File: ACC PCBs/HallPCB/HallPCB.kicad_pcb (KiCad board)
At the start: 2 copper layers, 22.8 x 11.3 mm, 3 parts, among them J1 Conn_01x04_Socket, U2 AP2127N-1.0

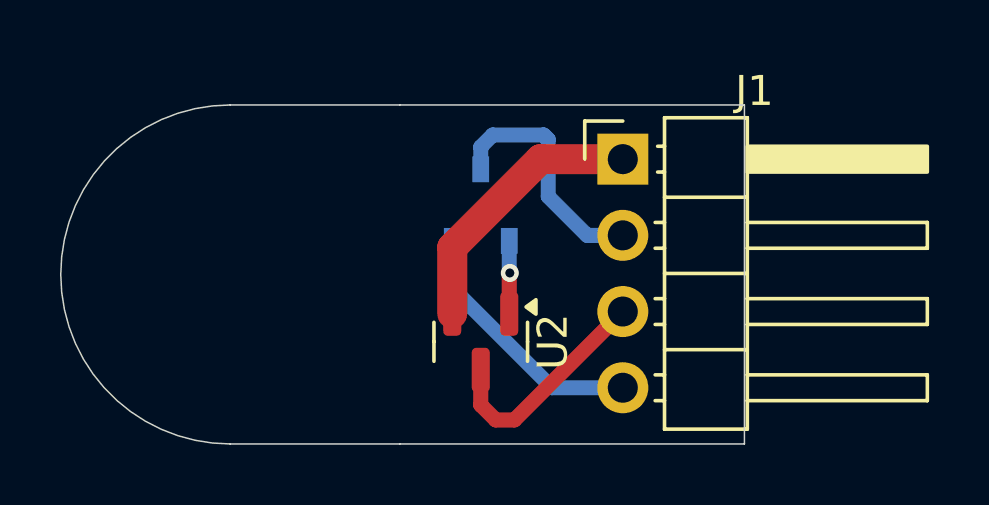
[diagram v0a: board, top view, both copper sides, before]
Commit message: post R1 - flipped many traces and worked on adding an internal sensor for reduncancy
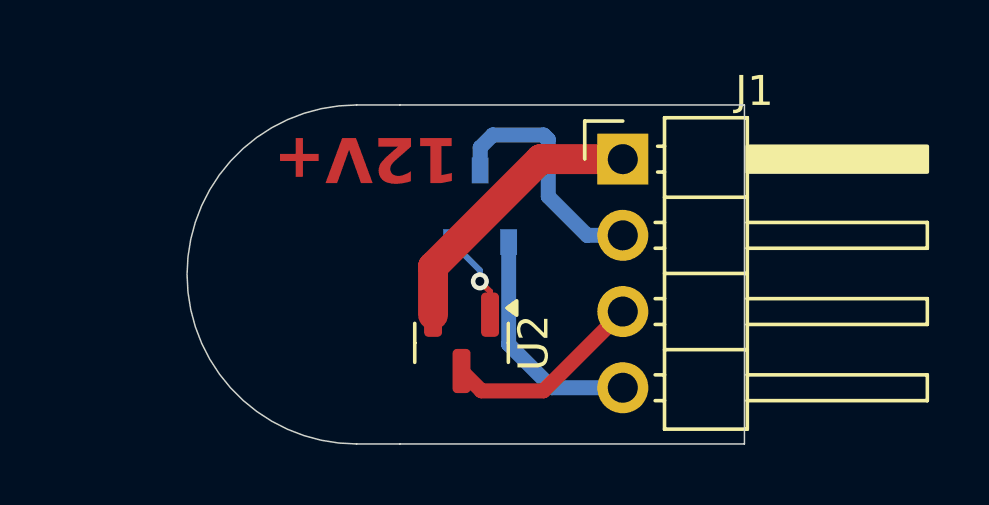
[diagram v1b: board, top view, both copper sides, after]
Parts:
- moved U2 0.64 mm to (135.4, 85.6)
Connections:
- HALL pad 1: SIG -> VOUT
- HALL pad 2: VOUT -> SIG
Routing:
- net RAWSWPOWER: track 7.61 -> 6.74 mm
- net VOUT: track 8.63 -> 7.81 mm
- net SIG: track 2.44 -> 2.95 mm
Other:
- board size 22.8 x 11.3 mm -> 18.6 x 11.3 mm
- board text added: "12V+"
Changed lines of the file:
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@@
 			(drillshape 0)
 			(scaleselection 1)
-			(outputdirectory "FAB/")
+			(outputdirectory "../../../Downloads/PWROUTPUT/")
 		)
 	)
@@
 	(footprint "Package_TO_SOT_SMD:SOT-23"
 		(layer "F.Cu")
-		(at 136 85.5947 -90)
+		(at 135.36 85.63 -90)
 		(descr "SOT, 3 Pin (JEDEC TO-236 Var AB https://www.jedec.org/document_search?search_api_views_fulltext=TO-236), generated with kicad-footprint-generator ipc_gullwing_generator.py")
 		(tags "SOT TO_SOT_SMD")
@@
 	(footprint "TLE49643MXTMA1:PG-SOT23-3-15_INF"
 		(layer "B.Cu")
-		(at 136 81.0385 90)
+		(at 135.980001 81.0762 90)
 		(tags "TLE49643MXTMA1 ")
 		(property "Reference" "HALL"
-			(at 0 0 0)
+			(at 0 -2.440001 270)
 			(unlocked yes)
 			(layer "B.SilkS")
@@
 		)
 		(property "Datasheet" "https://www.infineon.com/dgdl/Infineon-TLE4964_3M-DS-v01_00-en.pdf?fileId=db3a30433cabdd35013cc94b7c0f64f9"
-			(at 0 0 270)
+			(at 0 0 90)
 			(layer "B.Fab")
 			(hide yes)
@@
 		)
 		(property "Description" ""
-			(at 0 0 270)
+			(at 0 0 90)
 			(layer "B.Fab")
 			(hide yes)
@@
 		(attr smd)
 		(fp_line
+			(start 0.8255 -1.6256)
+			(end 0.8255 -0.61214)
+			(stroke
+				(width 0.1524)
+				(type solid)
+			)
+			(layer "B.SilkS")
+		)
+		(fp_line
+			(start -0.8255 -1.6256)
+			(end 0.8255 -1.6256)
+			(stroke
+				(width 0.1524)
+				(type solid)
+			)
+			(layer "B.SilkS")
+		)
+		(fp_line
 			(start -0.8255 0.337861)
 			(end -0.8255 -0.337861)
+			(stroke
+				(width 0.1524)
+				(type solid)
+			)
+			(layer "B.SilkS")
+		)
+		(fp_line
+			(start 0.8255 0.61214)
+			(end 0.8255 1.6256)
+			(stroke
+				(width 0.1524)
+				(type solid)
+			)
+			(layer "B.SilkS")
+		)
+		(fp_line
+			(start 0.8255 1.6256)
+			(end -0.8255 1.6256)
 			(stroke
 				(width 0.1524)
@@
 		)
 		(fp_text user "*"
+			(at -1.4478 2.6518 90)
+			(layer "B.SilkS")
+			(effects
+				(font
+					(size 1 1)
+					(thickness 0.15)
+				)
+				(justify mirror)
+			)
+		)
+		(fp_text user "*"
 			(at -1.4478 2.6518 270)
 			(unlocked yes)
@@
 			)
 		)
+		(fp_text user "${REFERENCE}"
+			(at 0 0 270)
+			(unlocked yes)
+			(layer "B.Fab")
+			(effects
+				(font
+					(size 1 1)
+					(thickness 0.15)
+				)
+				(justify mirror)
+			)
+		)
 		(fp_text user "*"
-			(at -1.4478 2.6518 270)
-			(layer "B.SilkS")
+			(at -0.3175 1.4224 90)
+			(layer "B.Fab")
 			(effects
 				(font
@@
 		(fp_text user "*"
 			(at -0.3175 1.4224 270)
-			(unlocked yes)
-			(layer "B.Fab")
-			(effects
-				(font
-					(size 1 1)
-					(thickness 0.15)
-				)
-				(justify mirror)
-			)
-		)
-		(fp_text user "*"
-			(at -0.3175 1.4224 270)
-			(layer "B.Fab")
-			(effects
-				(font
-					(size 1 1)
-					(thickness 0.15)
-				)
-				(justify mirror)
-			)
-		)
-		(fp_text user "${REFERENCE}"
-			(at 0 0 270)
 			(unlocked yes)
 			(layer "B.Fab")
@@
 			(size 0.8636 0.5588)
 			(layers "B.Cu" "B.Mask" "B.Paste")
-			(net 5 "SIG")
+			(net 2 "VOUT")
 			(pinfunction "VDD")
 			(pintype "power_in")
@@
 			(size 0.8636 0.5588)
 			(layers "B.Cu" "B.Mask" "B.Paste")
-			(net 2 "VOUT")
+			(net 5 "SIG")
 			(pinfunction "Q")
 			(pintype "output")
@@
 	)
 	(gr_line
+		(start 133.3 89)
+		(end 131.86 89)
+		(stroke
+			(width 0.05)
+			(type default)
+		)
+		(layer "Edge.Cuts")
+	)
+	(gr_line
 		(start 144.789524 89)
 		(end 144.789524 77.7)
@@
 	)
 	(gr_line
-		(start 127.65 77.7)
-		(end 133.3 77.7)
-		(stroke
-			(width 0.05)
-			(type default)
-		)
-		(layer "Edge.Cuts")
-	)
-	(gr_line
-		(start 127.65 89)
-		(end 133.3 89)
+		(start 133.3 77.7)
+		(end 131.86 77.7)
 		(stroke
 			(width 0.05)
@@
 	)
 	(gr_arc
-		(start 127.65 89)
-		(mid 122 83.35)
-		(end 127.65 77.7)
+		(start 131.86 89)
+		(mid 126.21 83.35)
+		(end 131.86 77.7)
 		(stroke
 			(width 0.05)
@@
 		)
 		(layer "Edge.Cuts")
+	)
+	(gr_text "12V+\n"
+		(at 135.27 78.62 180)
+		(layer "F.Cu")
+		(effects
+			(font
+				(size 1.5 1.5)
+				(thickness 0.3)
+				(bold yes)
+			)
+			(justify left bottom)
+		)
+	)
+	(segment
+		(start 136.4 78.7)
+		(end 135.980001 79.119999)
+		(width 0.5)
+		(layer "B.Cu")
+		(net 1)
+	)
+	(segment
+		(start 140.7354 82.0462)
+		(end 139.5462 82.0462)
+		(width 0.5)
+		(layer "B.Cu")
+		(net 1)
+	)
+	(segment
+		(start 138.25 80.75)
+		(end 138.25 78.85)
+		(width 0.5)
+		(layer "B.Cu")
+		(net 1)
+	)
+	(segment
+		(start 138.1 78.7)
+		(end 136.4 78.7)
+		(width 0.5)
+		(layer "B.Cu")
+		(net 1)
+	)
+	(segment
+		(start 135.980001 79.119999)
+		(end 135.980001 79.8824)
+		(width 0.5)
+		(layer "B.Cu")
+		(net 1)
+	)
+	(segment
+		(start 139.5462 82.0462)
+		(end 138.25 80.75)
+		(width 0.5)
+		(layer "B.Cu")
+		(net 1)
 	)
 	(segment
@@
 	)
 	(segment
-		(start 139.5462 82.0462)
-		(end 138.25 80.75)
-		(width 0.5)
-		(layer "B.Cu")
-		(net 1)
-	)
-	(segment
-		(start 136.4 78.7)
-		(end 136 79.1)
-		(width 0.5)
-		(layer "B.Cu")
-		(net 1)
-	)
-	(segment
-		(start 138.1 78.7)
-		(end 136.4 78.7)
-		(width 0.5)
-		(layer "B.Cu")
-		(net 1)
-	)
-	(segment
-		(start 136 79.1)
-		(end 136 79.8447)
-		(width 0.5)
-		(layer "B.Cu")
-		(net 1)
-	)
-	(segment
-		(start 140.7354 82.0462)
-		(end 139.5462 82.0462)
-		(width 0.5)
-		(layer "B.Cu")
-		(net 1)
-	)
-	(segment
-		(start 138.25 80.75)
-		(end 138.25 78.85)
-		(width 0.5)
-		(layer "B.Cu")
-		(net 1)
-	)
-	(segment
-		(start 135.049999 83.799999)
-		(end 135.049999 82.2323)
+		(start 136.930002 85.680002)
+		(end 136.930002 82.27)
 		(width 0.5)
 		(layer "B.Cu")
@@
 	(segment
 		(start 138.3762 87.1262)
-		(end 135.049999 83.799999)
+		(end 136.930002 85.680002)
 		(width 0.5)
 		(layer "B.Cu")
@@
 	)
 	(segment
-		(start 140.7354 84.5862)
-		(end 137.1216 88.2)
+		(start 136.0225 87.23)
+		(end 135.36 86.5675)
 		(width 0.5)
 		(layer "F.Cu")
@@
 	)
 	(segment
-		(start 136 87.7)
-		(end 136 86.5322)
+		(start 138.0916 87.23)
+		(end 136.0225 87.23)
 		(width 0.5)
 		(layer "F.Cu")
@@
 	)
 	(segment
-		(start 137.1216 88.2)
-		(end 136.5 88.2)
+		(start 140.7354 84.5862)
+		(end 138.0916 87.23)
 		(width 0.5)
 		(layer "F.Cu")
@@
 	)
 	(segment
-		(start 136.5 88.2)
-		(end 136 87.7)
-		(width 0.5)
-		(layer "F.Cu")
-		(net 3)
-	)
-	(segment
-		(start 135.05 82.45)
-		(end 135.05 84.6572)
-		(width 1)
-		(layer "F.Cu")
-		(net 4)
-	)
-	(segment
-		(start 135.05 82.45)
-		(end 137.9938 79.5062)
+		(start 134.41 83.09)
+		(end 134.41 84.6925)
 		(width 1)
 		(layer "F.Cu")
@@
 	)
 	(segment
-		(start 137.9938 79.5062)
-		(end 140.7354 79.5062)
+		(start 140.7354 79.5062)
+		(end 137.9938 79.5062)
 		(width 1)
 		(layer "F.Cu")
@@
 	)
 	(segment
-		(start 136.95 83.318964)
-		(end 136.968964 83.3)
-		(width 0.5)
+		(start 137.9938 79.5062)
+		(end 134.41 83.09)
+		(width 1)
+		(layer "F.Cu")
+		(net 4)
+	)
+	(segment
+		(start 136.31 84.6925)
+		(end 136.31 83.92)
+		(width 0.2)
 		(layer "F.Cu")
 		(net 5)
 	)
 	(segment
-		(start 136.95 84.6572)
-		(end 136.95 83.318964)
-		(width 0.5)
+		(start 136.31 83.92)
+		(end 135.97 83.58)
+		(width 0.2)
 		(layer "F.Cu")
 		(net 5)
 	)
 	(via
-		(at 136.968964 83.3)
+		(at 135.97 83.58)
 		(size 0.6)
 		(drill 0.3)
 		(layers "F.Cu" "B.Cu")
-		(free yes)
 		(net 5)
 	)
 	(segment
-		(start 136.950001 82.2323)
-		(end 136.950001 83.281037)
-		(width 0.5)
+		(start 135.97 83.58)
+		(end 135.97 83.21)
+		(width 0.2)
 		(layer "B.Cu")
 		(net 5)
 	)
 	(segment
-		(start 136.950001 83.281037)
-		(end 136.968964 83.3)
-		(width 0.5)
+		(start 135.97 83.21)
+		(end 135.03 82.27)
+		(width 0.2)
 		(layer "B.Cu")
 		(net 5)
 	)
 	(group ""
-		(members "3065ad7f-c137-40a3-84d3-ba645962e42f" "500b3212-06de-4e9d-b3e0-fe4867ded8ce")
+		(members "3065ad7f-c137-40a3-84d3-ba645962e42f")
 	)
 	(embedded_fonts no)
